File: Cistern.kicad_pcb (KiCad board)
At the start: 2 copper layers, 55.5 x 79.6 mm, 16 parts, among them J2 Gauge Stepper, J3 Power Connector, Q1 BD244C, Q2 Gauge Calibration, SW1 WiFi reset, SW2 Water Sensor, U1 ULN2003A, U3 Boost Converter (5->20 V)

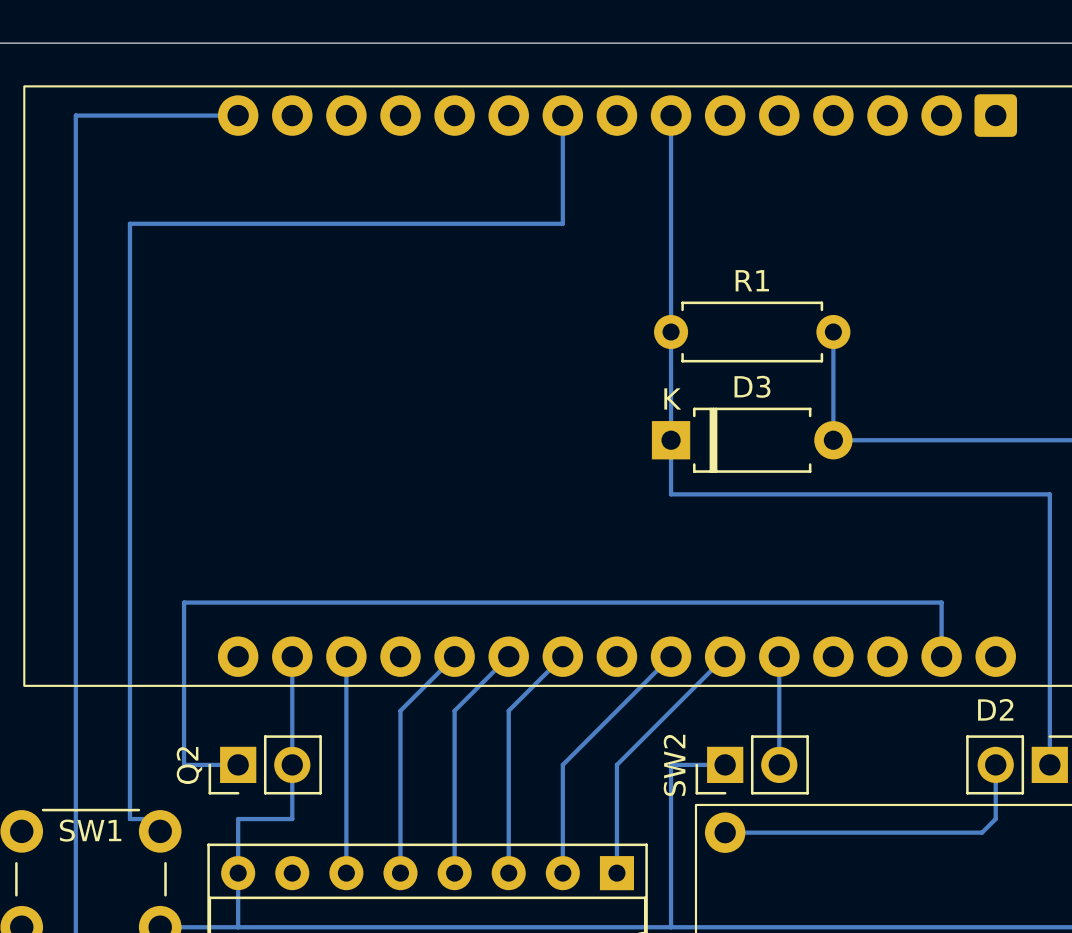
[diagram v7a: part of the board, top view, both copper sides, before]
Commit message: Changing pin assignments some more, adding gauge calibration sensor
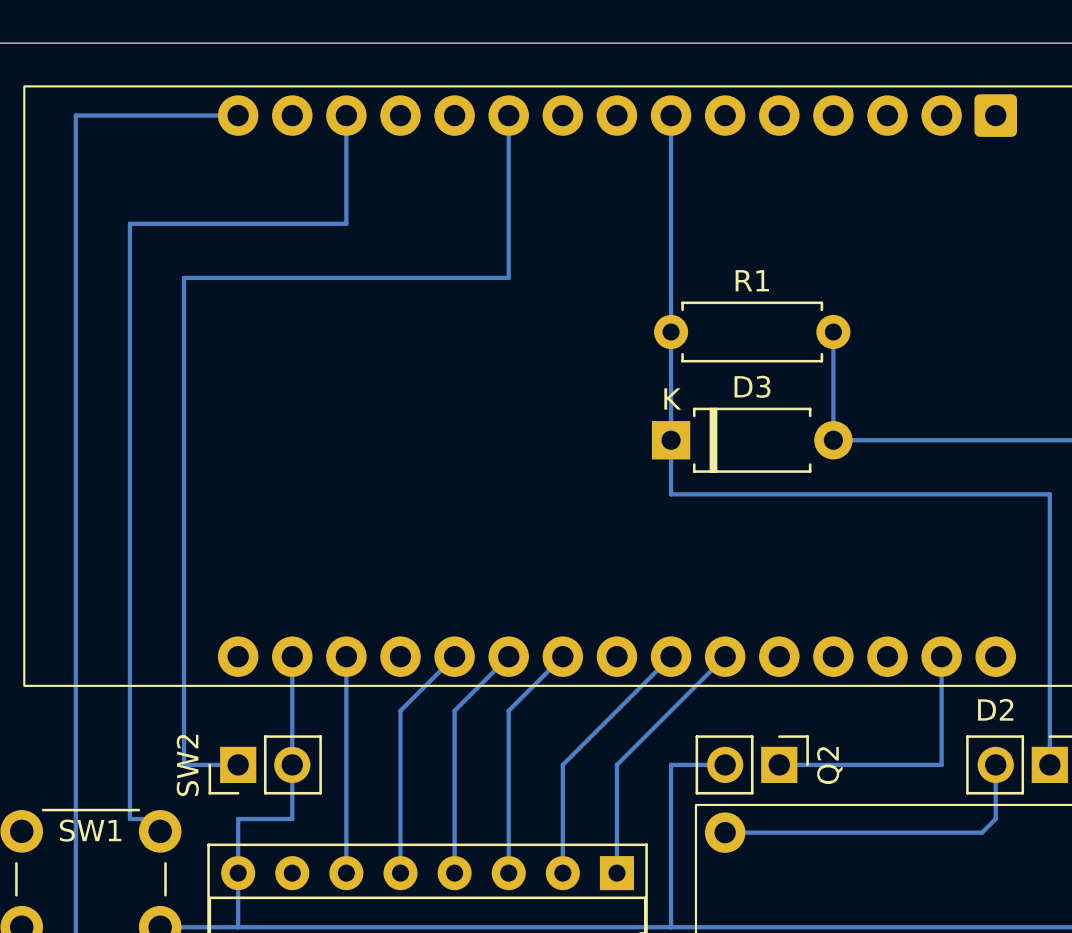
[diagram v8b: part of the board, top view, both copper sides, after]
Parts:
- moved Q2 25.4 mm to (78.7, 55.9), turned to -90 degrees
- moved SW2 22.9 mm to (53.3, 55.9)
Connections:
- MCU1 pad 10: unconnected-(MCU1-GPIO27-Pad10) -> Net-(MCU1-GPIO27)
- MCU1 pad 13: unconnected-(MCU1-GPIO13-Pad13) -> Net-(MCU1-GPIO13)
- MCU1 pad 20: Net-(MCU1-GPIO21) -> unconnected-(MCU1-GPIO21-Pad20)
- MCU1 pad 9: Net-(MCU1-GPIO26) -> unconnected-(MCU1-GPIO26-Pad9)
- SW1 pad 1: Net-(MCU1-GPIO26) -> Net-(MCU1-GPIO13)
- SW2 pad 1: GND -> Net-(MCU1-GPIO27)
- SW2 pad 2: Net-(MCU1-GPIO21) -> GND
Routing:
- net Net-(MCU1-GPIO26): track 55.0 -> 0.00 mm
- net Net-(MCU1-GPIO27): track 0.00 -> 48.3 mm
- net Net-(MCU1-GPIO13): track 0.00 -> 44.8 mm
- net Net-(MCU1-GPIO22): track 48.3 -> 12.7 mm
- net Net-(MCU1-GPIO21): track 5.08 -> 0.00 mm
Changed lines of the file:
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@@
 	(net 9 "Net-(J2-Pin_3)")
 	(net 10 "Net-(J2-Pin_2)")
-	(net 11 "Net-(MCU1-GPIO26)")
+	(net 11 "unconnected-(MCU1-GPIO21-Pad20)")
 	(net 12 "Net-(MCU1-TX2)")
 	(net 13 "unconnected-(MCU1-GPIO2-Pad27)")
@@
 	(net 17 "unconnected-(MCU1-VN-Pad3)")
 	(net 18 "unconnected-(MCU1-3V3-Pad30)")
-	(net 19 "unconnected-(MCU1-GPIO13-Pad13)")
+	(net 19 "Net-(MCU1-GPIO13)")
 	(net 20 "Net-(MCU1-GPIO19)")
-	(net 21 "unconnected-(MCU1-GPIO27-Pad10)")
+	(net 21 "Net-(MCU1-GPIO27)")
 	(net 22 "Net-(MCU1-GPIO22)")
 	(net 23 "unconnected-(MCU1-GPIO23-Pad16)")
@@
 	(net 38 "unconnected-(MCU1-GPIO5-Pad23)")
 	(net 39 "Net-(MCU1-GPIO15)")
-	(net 40 "Net-(MCU1-GPIO21)")
+	(net 40 "unconnected-(MCU1-GPIO26-Pad9)")
 	(net 41 "unconnected-(MCU1-GPIO34-Pad4)")
 	(net 42 "unconnected-(MCU1-GND-Pad14)")
 	(footprint "Connector_PinHeader_2.54mm:PinHeader_1x02_P2.54mm_Vertical"
 		(layer "F.Cu")
-		(at 76.2 55.88 90)
+		(at 53.34 55.88 90)
 		(descr "Through hole straight pin header, 1x02, 2.54mm pitch, single row")
 		(tags "Through hole pin header THT 1x02 2.54mm single row")
@@
 		)
 		(property "Value" "Water Sensor"
-			(at 0 -7.62 360)
+			(at 0 -7.62 0)
 			(layer "F.Fab")
 			(effects
@@
 		)
 		(fp_text user "${REFERENCE}"
-			(at 0 1.27 360)
+			(at 0 1.27 0)
 			(layer "F.Fab")
 			(effects
@@
 			(layers "*.Cu" "*.Mask")
 			(remove_unused_layers no)
-			(net 6 "GND")
+			(net 21 "Net-(MCU1-GPIO27)")
 			(pinfunction "A")
 			(pintype "passive")
@@
 			(layers "*.Cu" "*.Mask")
 			(remove_unused_layers no)
-			(net 40 "Net-(MCU1-GPIO21)")
+			(net 6 "GND")
 			(pinfunction "B")
 			(pintype "passive")
@@
 			(layers "*.Cu" "*.Mask")
 			(remove_unused_layers no)
-			(net 11 "Net-(MCU1-GPIO26)")
+			(net 19 "Net-(MCU1-GPIO13)")
 			(pinfunction "1")
 			(pintype "passive")
@@
 			(layers "*.Cu" "*.Mask")
 			(remove_unused_layers no)
-			(net 11 "Net-(MCU1-GPIO26)")
+			(net 19 "Net-(MCU1-GPIO13)")
 			(pinfunction "1")
 			(pintype "passive")
@@
 			(net 41 "unconnected-(MCU1-GPIO34-Pad4)")
 			(pinfunction "GPIO34")
-			(pintype "bidirectional")
+			(pintype "bidirectional+no_connect")
 		)
 		(pad "5" thru_hole circle
@@
 			(layers "*.Cu" "*.Mask")
 			(remove_unused_layers no)
-			(net 11 "Net-(MCU1-GPIO26)")
+			(net 40 "unconnected-(MCU1-GPIO26-Pad9)")
 			(pinfunction "GPIO26")
-			(pintype "bidirectional")
+			(pintype "bidirectional+no_connect")
 		)
 		(pad "10" thru_hole circle
@@
 			(layers "*.Cu" "*.Mask")
 			(remove_unused_layers no)
-			(net 21 "unconnected-(MCU1-GPIO27-Pad10)")
+			(net 21 "Net-(MCU1-GPIO27)")
 			(pinfunction "GPIO27")
-			(pintype "bidirectional+no_connect")
+			(pintype "bidirectional")
 		)
 		(pad "11" thru_hole circle
@@
 			(layers "*.Cu" "*.Mask")
 			(remove_unused_layers no)
-			(net 19 "unconnected-(MCU1-GPIO13-Pad13)")
+			(net 19 "Net-(MCU1-GPIO13)")
 			(pinfunction "GPIO13")
-			(pintype "bidirectional+no_connect")
+			(pintype "bidirectional")
 		)
 		(pad "14" thru_hole circle
@@
 			(layers "*.Cu" "*.Mask")
 			(remove_unused_layers no)
-			(net 40 "Net-(MCU1-GPIO21)")
+			(net 11 "unconnected-(MCU1-GPIO21-Pad20)")
 			(pinfunction "GPIO21")
-			(pintype "bidirectional")
+			(pintype "bidirectional+no_connect")
 		)
 		(pad "21" thru_hole circle
@@
 	(footprint "Connector_PinHeader_2.54mm:PinHeader_1x02_P2.54mm_Vertical"
 		(layer "F.Cu")
-		(at 53.34 55.88 90)
+		(at 78.74 55.88 -90)
 		(descr "Through hole straight pin header, 1x02, 2.54mm pitch, single row")
 		(tags "Through hole pin header THT 1x02 2.54mm single row")
@@
 		)
 		(property "Footprint" "Connector_PinHeader_2.54mm:PinHeader_1x02_P2.54mm_Vertical"
-			(at 0 0 90)
+			(at 0 0 -90)
 			(unlocked yes)
 			(layer "F.Fab")
@@
 		)
 		(property "Datasheet" ""
-			(at 0 0 90)
+			(at 0 0 -90)
 			(unlocked yes)
 			(layer "F.Fab")
@@
 		)
 		(property "Description" "NPN phototransistor, collector/emitter"
-			(at 0 0 90)
+			(at 0 0 -90)
 			(unlocked yes)
 			(layer "F.Fab")
@@
 		(attr through_hole)
 		(fp_line
-			(start -1.33 -1.33)
-			(end 0 -1.33)
+			(start -1.33 3.87)
+			(end 1.33 3.87)
 			(stroke
 				(width 0.12)
@@
 		)
 		(fp_line
-			(start -1.33 0)
-			(end -1.33 -1.33)
+			(start -1.33 1.27)
+			(end -1.33 3.87)
 			(stroke
 				(width 0.12)
@@
 		)
 		(fp_line
-			(start 1.33 1.27)
-			(end 1.33 3.87)
+			(start -1.33 1.27)
+			(end 1.33 1.27)
 			(stroke
 				(width 0.12)
@@
 		)
 		(fp_line
-			(start -1.33 1.27)
-			(end 1.33 1.27)
+			(start 1.33 1.27)
+			(end 1.33 3.87)
 			(stroke
 				(width 0.12)
@@
 		)
 		(fp_line
-			(start -1.33 1.27)
-			(end -1.33 3.87)
+			(start -1.33 0)
+			(end -1.33 -1.33)
 			(stroke
 				(width 0.12)
@@
 		)
 		(fp_line
-			(start -1.33 3.87)
-			(end 1.33 3.87)
+			(start -1.33 -1.33)
+			(end 0 -1.33)
 			(stroke
 				(width 0.12)
@@
 		)
 		(fp_line
-			(start 1.8 -1.8)
-			(end -1.8 -1.8)
+			(start -1.8 4.35)
+			(end 1.8 4.35)
 			(stroke
 				(width 0.05)
@@
 		)
 		(fp_line
-			(start -1.8 -1.8)
-			(end -1.8 4.35)
+			(start 1.8 4.35)
+			(end 1.8 -1.8)
 			(stroke
 				(width 0.05)
@@
 		)
 		(fp_line
-			(start 1.8 4.35)
-			(end 1.8 -1.8)
+			(start -1.8 -1.8)
+			(end -1.8 4.35)
 			(stroke
 				(width 0.05)
@@
 		)
 		(fp_line
-			(start -1.8 4.35)
-			(end 1.8 4.35)
+			(start 1.8 -1.8)
+			(end -1.8 -1.8)
 			(stroke
 				(width 0.05)
@@
 		)
 		(fp_line
-			(start 1.27 -1.27)
-			(end 1.27 3.81)
+			(start -1.27 3.81)
+			(end -1.27 -0.635)
 			(stroke
 				(width 0.1)
@@
 		)
 		(fp_line
-			(start -0.635 -1.27)
-			(end 1.27 -1.27)
+			(start 1.27 3.81)
+			(end -1.27 3.81)
 			(stroke
 				(width 0.1)
@@
 		)
 		(fp_line
-			(start 1.27 3.81)
-			(end -1.27 3.81)
+			(start -0.635 -1.27)
+			(end 1.27 -1.27)
 			(stroke
 				(width 0.1)
@@
 		)
 		(fp_line
-			(start -1.27 3.81)
-			(end -1.27 -0.635)
+			(start 1.27 -1.27)
+			(end 1.27 3.81)
 			(stroke
 				(width 0.1)
@@
 		)
 		(pad "1" thru_hole rect
-			(at 0 0 90)
+			(at 0 0 270)
 			(size 1.7 1.7)
 			(drill 1)
@@
 		)
 		(pad "2" thru_hole oval
-			(at 0 2.54 90)
+			(at 0 2.54 270)
 			(size 1.7 1.7)
 			(drill 1)
@@
 	)
 	(segment
-		(start 49.1 58.42)
-		(end 48.26 58.42)
+		(start 66.04 53.34)
+		(end 68.58 50.8)
 		(width 0.2)
 		(layer "B.Cu")
-		(net 11)
+		(net 12)
 	)
 	(segment
-		(start 48.26 30.48)
-		(end 68.58 30.48)
+		(start 66.04 60.96)
+		(end 66.04 53.34)
 		(width 0.2)
 		(layer "B.Cu")
-		(net 11)
+		(net 12)
 	)
 	(segment
-		(start 49.68 59)
-		(end 49.1 58.42)
+		(start 63.5 53.34)
+		(end 66.04 50.8)
 		(width 0.2)
 		(layer "B.Cu")
-		(net 11)
+		(net 15)
 	)
 	(segment
-		(start 48.26 58.42)
-		(end 48.26 30.48)
+		(start 63.5 60.96)
+		(end 63.5 53.34)
 		(width 0.2)
 		(layer "B.Cu")
-		(net 11)
+		(net 15)
 	)
 	(segment
-		(start 68.58 30.48)
-		(end 68.58 25.4)
+		(start 49.1 58.42)
+		(end 48.26 58.42)
 		(width 0.2)
 		(layer "B.Cu")
-		(net 11)
+		(net 19)
 	)
 	(segment
-		(start 66.04 53.34)
-		(end 68.58 50.8)
+		(start 58.42 30.48)
+		(end 58.42 25.4)
 		(width 0.2)
 		(layer "B.Cu")
-		(net 12)
+		(net 19)
 	)
 	(segment
-		(start 66.04 60.96)
-		(end 66.04 53.34)
+		(start 48.26 30.48)
+		(end 58.42 30.48)
 		(width 0.2)
 		(layer "B.Cu")
-		(net 12)
+		(net 19)
 	)
 	(segment
-		(start 63.5 53.34)
-		(end 66.04 50.8)
+		(start 49.68 59)
+		(end 49.1 58.42)
 		(width 0.2)
 		(layer "B.Cu")
-		(net 15)
+		(net 19)
 	)
 	(segment
-		(start 63.5 60.96)
-		(end 63.5 53.34)
+		(start 48.26 58.42)
+		(end 48.26 30.48)
 		(width 0.2)
 		(layer "B.Cu")
-		(net 15)
+		(net 19)
 	)
 	(segment
@@
 	)
 	(segment
+		(start 50.8 55.88)
+		(end 50.8 33.02)
+		(width 0.2)
+		(layer "B.Cu")
+		(net 21)
+	)
+	(segment
 		(start 53.34 55.88)
 		(end 50.8 55.88)
 		(width 0.2)
 		(layer "B.Cu")
-		(net 22)
+		(net 21)
 	)
 	(segment
-		(start 86.36 48.26)
-		(end 86.36 50.8)
+		(start 66.04 33.02)
+		(end 66.04 25.4)
 		(width 0.2)
 		(layer "B.Cu")
-		(net 22)
+		(net 21)
 	)
 	(segment
-		(start 50.8 55.88)
-		(end 50.8 48.26)
+		(start 50.8 33.02)
+		(end 66.04 33.02)
+		(width 0.2)
+		(layer "B.Cu")
+		(net 21)
+	)
+	(segment
+		(start 78.74 55.88)
+		(end 86.36 55.88)
 		(width 0.2)
 		(layer "B.Cu")
@@
 	)
 	(segment
-		(start 50.8 48.26)
-		(end 86.36 48.26)
+		(start 86.36 55.88)
+		(end 86.36 50.8)
 		(width 0.2)
 		(layer "B.Cu")
@@
 		(net 39)
 	)
-	(segment
-		(start 78.74 50.8)
-		(end 78.74 55.88)
-		(width 0.2)
-		(layer "B.Cu")
-		(net 40)
-	)
 )
